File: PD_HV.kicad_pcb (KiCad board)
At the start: 4 copper layers, 100 x 85 mm, 83 parts, among them J1 USB_C_Receptacle, J2 USB_C_Receptacle, J3 Conn_Coaxial, Q1 AON7296, Q2 AON7410, Q3 AO3400A, SW1 SW_SPST, SW2 SW_SPST, SW3 SW_SPST, U2 LT3750A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

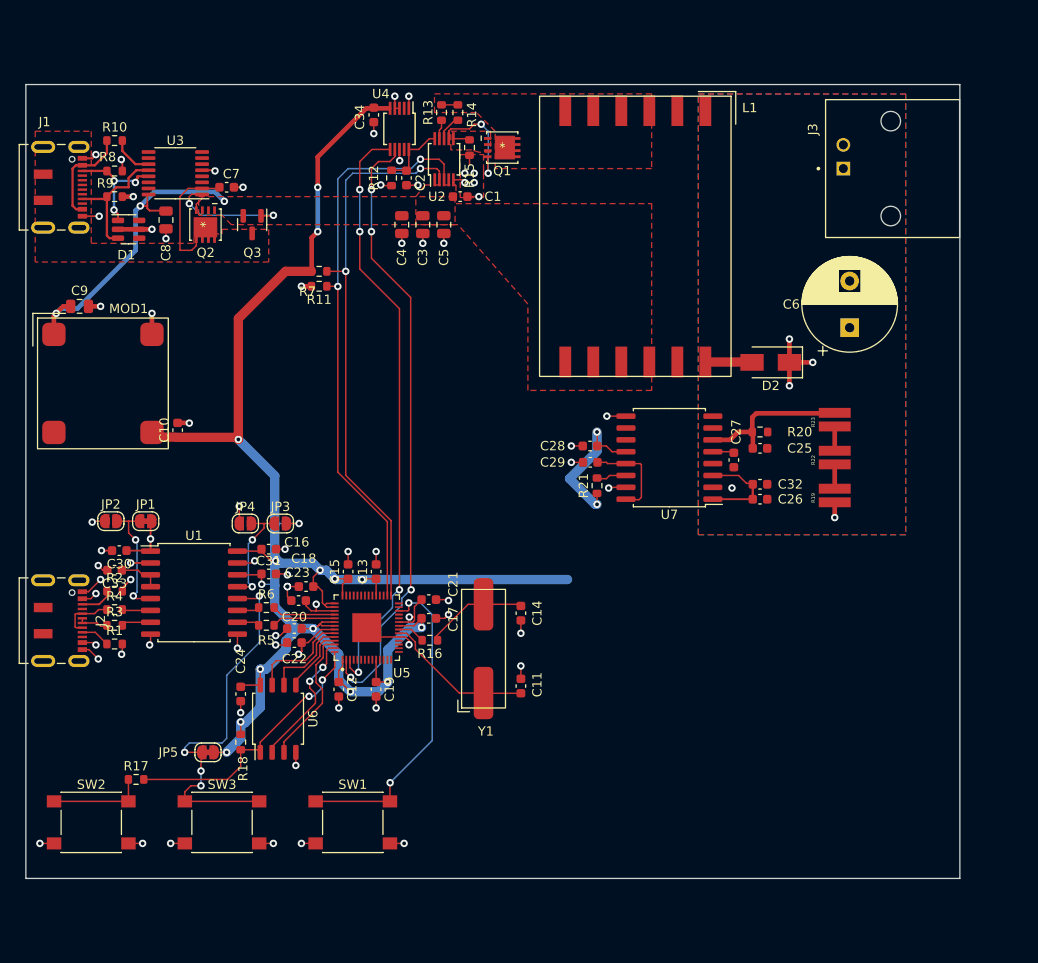
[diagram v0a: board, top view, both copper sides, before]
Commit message: finished routing, sending to fab
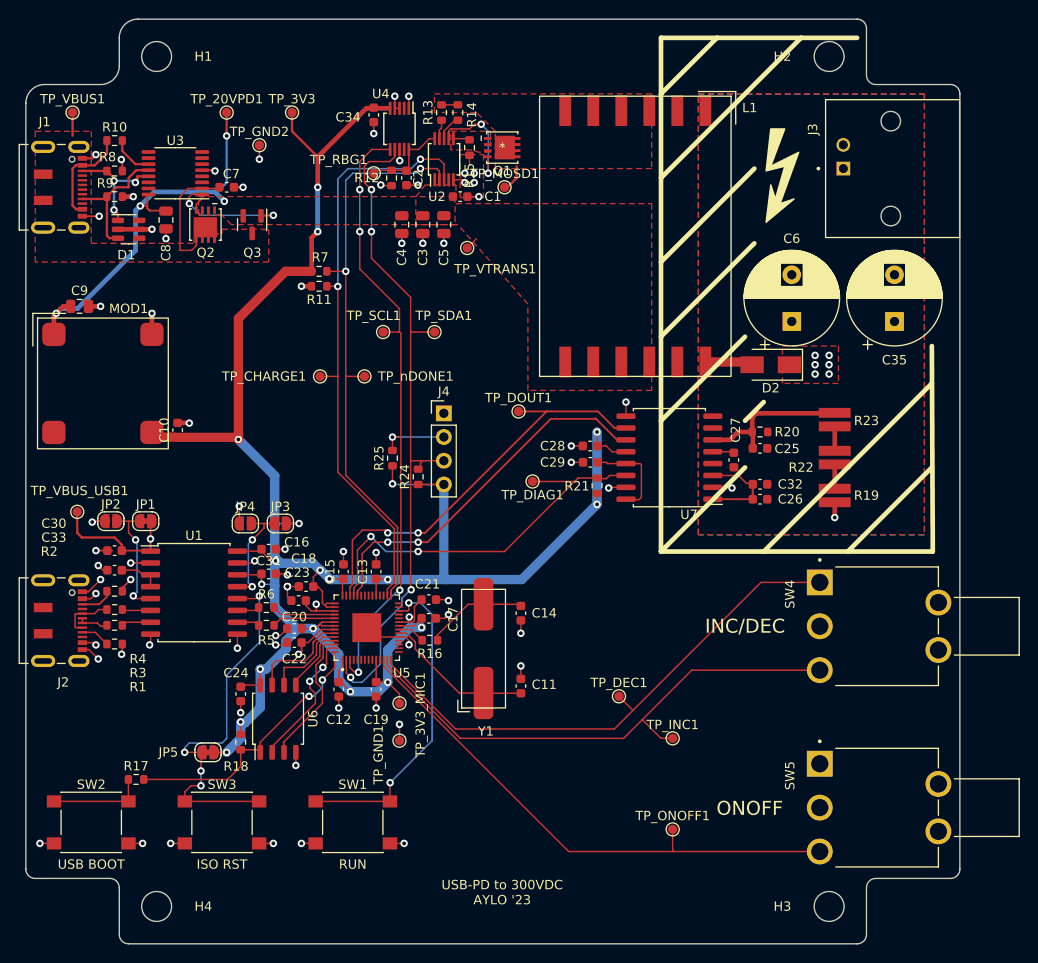
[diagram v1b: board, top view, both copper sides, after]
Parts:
- added C35: 3.3u, Capacitor_THT:CP_Radial_D10.0mm_P5.00mm, F.Cu at (167.0, 69.4)
- added H1: MountingHole, MountingHole:MountingHole_3.2mm_M3, F.Cu at (88.0, 41.0)
- added H2: MountingHole, MountingHole:MountingHole_3.2mm_M3, F.Cu at (160.0, 41.0)
- added H3: MountingHole, MountingHole:MountingHole_3.2mm_M3, F.Cu at (160.0, 132.0)
- added H4: MountingHole, MountingHole:MountingHole_3.2mm_M3, F.Cu at (88.0, 132.0)
- added J4: Conn_01x04_Male, Connector_PinHeader_2.54mm:PinHeader_1x04_P2.54mm_Vertical, F.Cu at (118.8, 79.2)
- added R24: 4k7, Resistor_SMD:R_0603_1608Metric, F.Cu at (116.0, 86.0)
- added R25: 4k7, Resistor_SMD:R_0603_1608Metric, F.Cu at (113.2, 84.0)
- added REF**: IEC_HV, PD_HV_footprints:IEC_HV, F.Cu at (154.8, 52.8)
- added SW4: MOM-OFF-MOM, PD_HV_footprints:SW_100SP1T2B4M6QE, F.Cu at (159.0, 102.0)
- added SW5: SW_SPDT, PD_HV_footprints:SW_100SP1T2B4M6QE, F.Cu at (159.0, 121.4)
- added TP_20VPD1: TestPoint, TestPoint:TestPoint_Pad_D1.0mm, F.Cu at (95.5, 47.0)
- added TP_3V3: TestPoint, TestPoint:TestPoint_Pad_D1.0mm, F.Cu at (102.5, 47.0)
- added TP_3V3_MIC1: TestPoint, TestPoint:TestPoint_Pad_D1.0mm, F.Cu at (114.0, 110.2)
- added TP_CHARGE1: TestPoint, TestPoint:TestPoint_Pad_D1.0mm, F.Cu at (105.5, 75.2)
- added TP_DEC1: TestPoint, TestPoint:TestPoint_Pad_D1.0mm, F.Cu at (137.5, 109.5)
- added TP_DIAG1: TestPoint, TestPoint:TestPoint_Pad_D1.0mm, F.Cu at (128.2, 86.5)
- added TP_DOUT1: TestPoint, TestPoint:TestPoint_Pad_D1.0mm, F.Cu at (126.8, 79.0)
- added TP_GND1: TestPoint, TestPoint:TestPoint_Pad_D1.0mm, F.Cu at (114.0, 114.2)
- added TP_GND2: TestPoint, TestPoint:TestPoint_Pad_D1.0mm, F.Cu at (99.0, 50.5)
- added TP_INC1: TestPoint, TestPoint:TestPoint_Pad_D1.0mm, F.Cu at (143.2, 114.0)
- added TP_MOSD1: TestPoint, TestPoint:TestPoint_Pad_D1.0mm, F.Cu at (125.2, 55.0)
- added TP_ONOFF1: TestPoint, TestPoint:TestPoint_Pad_D1.0mm, F.Cu at (143.2, 123.8)
- added TP_RBG1: TestPoint, TestPoint:TestPoint_Pad_D1.0mm, F.Cu at (111.2, 53.5)
- added TP_SCL1: TestPoint, TestPoint:TestPoint_Pad_D1.0mm, F.Cu at (112.2, 70.5)
- added TP_SDA1: TestPoint, TestPoint:TestPoint_Pad_D1.0mm, F.Cu at (117.8, 70.5)
- added TP_VBUS1: TestPoint, TestPoint:TestPoint_Pad_D1.0mm, F.Cu at (79.0, 47.0)
- added TP_VBUS_USB1: TestPoint, TestPoint:TestPoint_Pad_D1.0mm, F.Cu at (79.5, 89.8)
- added TP_VTRANS1: TestPoint, TestPoint:TestPoint_Pad_D1.0mm, F.Cu at (121.2, 61.5)
- added TP_nDONE1: TestPoint, TestPoint:TestPoint_Pad_D1.0mm, F.Cu at (110.2, 75.2)
- moved C6 6.24 mm to (156.0, 69.4)
- moved C15 0.50 mm to (108.0, 96.2)
- moved C30 0.50 mm to (83.5, 93.9)
- moved D2 0.25 mm to (153.8, 74.0)
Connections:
- net /HV_Flyback/SCL renamed /RP2040/SCL
- net /HV_Flyback/SDA renamed /RP2040/SDA
- U5 pad 12: unconnected-(U5-Pad12) -> /RP2040/ONOFF
- U5 pad 13: unconnected-(U5-Pad13) -> /RP2040/INC
- U5 pad 14: unconnected-(U5-Pad14) -> /RP2040/DEC
- U5 pad 38: unconnected-(U5-Pad38) -> /HVMeasurement/CLKIN
- U5 pad 39: unconnected-(U5-Pad39) -> /HVMeasurement/DIAG
- U5 pad 40: unconnected-(U5-Pad40) -> /HVMeasurement/DOUT
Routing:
- net /RP2040/ONOFF: track 0.00 -> 58.0 mm
- net /RP2040/DEC: track 0.00 -> 57.9 mm
- net /RP2040/INC: track 0.00 -> 57.2 mm
- net /HVMeasurement/DOUT: track 0.00 -> 45.0 mm, vias 0 -> 2
- net /HVMeasurement/CLKIN: track 0.00 -> 39.9 mm, vias 0 -> 2
- net /HVMeasurement/DIAG: track 3.17 -> 42.9 mm, vias 0 -> 2
- net +3.3V: track 216.8 -> 249.2 mm, vias 18 -> 19
- net +20V_USBPD: track 34.8 -> 46.5 mm, vias 3 -> 4
- net /RP2040/SCL: track 64.1 -> 73.8 mm, vias 4 -> 5
- net /RP2040/SDA: track 66.6 -> 75.0 mm
- net +VBUS_USB: track 8.83 -> 17.0 mm
- net +HV: track 9.13 -> 1.63 mm, vias 4 -> 7
- net Net-(L1-Pad3): track 1.75 -> 4.71 mm
- net GND: track 79.3 -> 81.9 mm, vias 56 -> 58
- net /HV_Flyback/CHARGE: track 62.1 -> 64.6 mm
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- added copper zone on F.Cu, net +HV
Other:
- board size 100 x 85 mm -> 100 x 99 mm
- board text added: "INC/DEC"
- board text added: "ISO RST"
- board text added: "ONOFF"
- board text added: "RUN"
- board text added: "USB BOOT"
- board text added: "USB-PD to 300VDC AYLO '23"
